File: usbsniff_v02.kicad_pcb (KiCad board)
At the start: 2 copper layers, 40 x 90 mm, 23 parts, among them P1 CONN_01X02, P2 CONN_01X08, P3 CONN_01X08, U1 AMS1117, U2 MAX3421E, U3 MAX3421E, X1 USB_type_A, X2 micro_USB, Y1 Crystal_Small, Y2 Crystal_Small

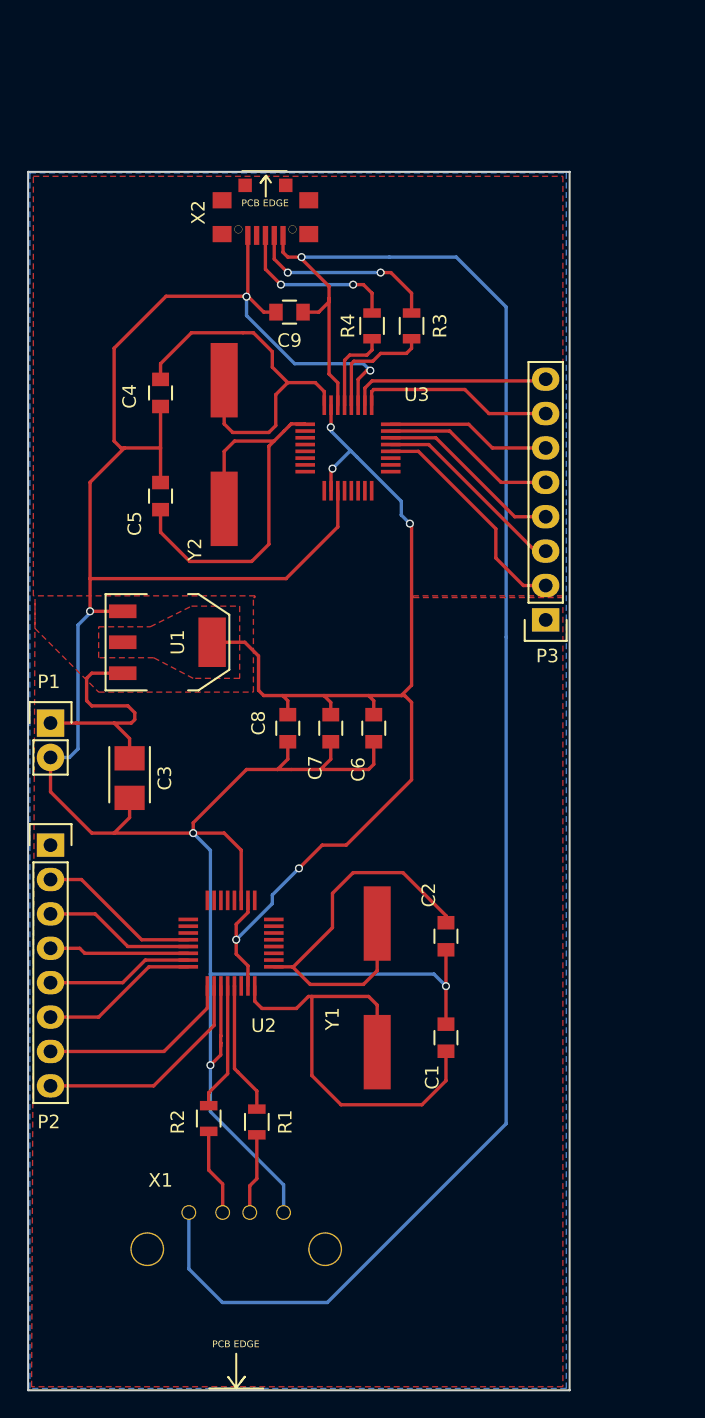
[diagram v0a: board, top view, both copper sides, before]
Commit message: add LED, redesign pcb
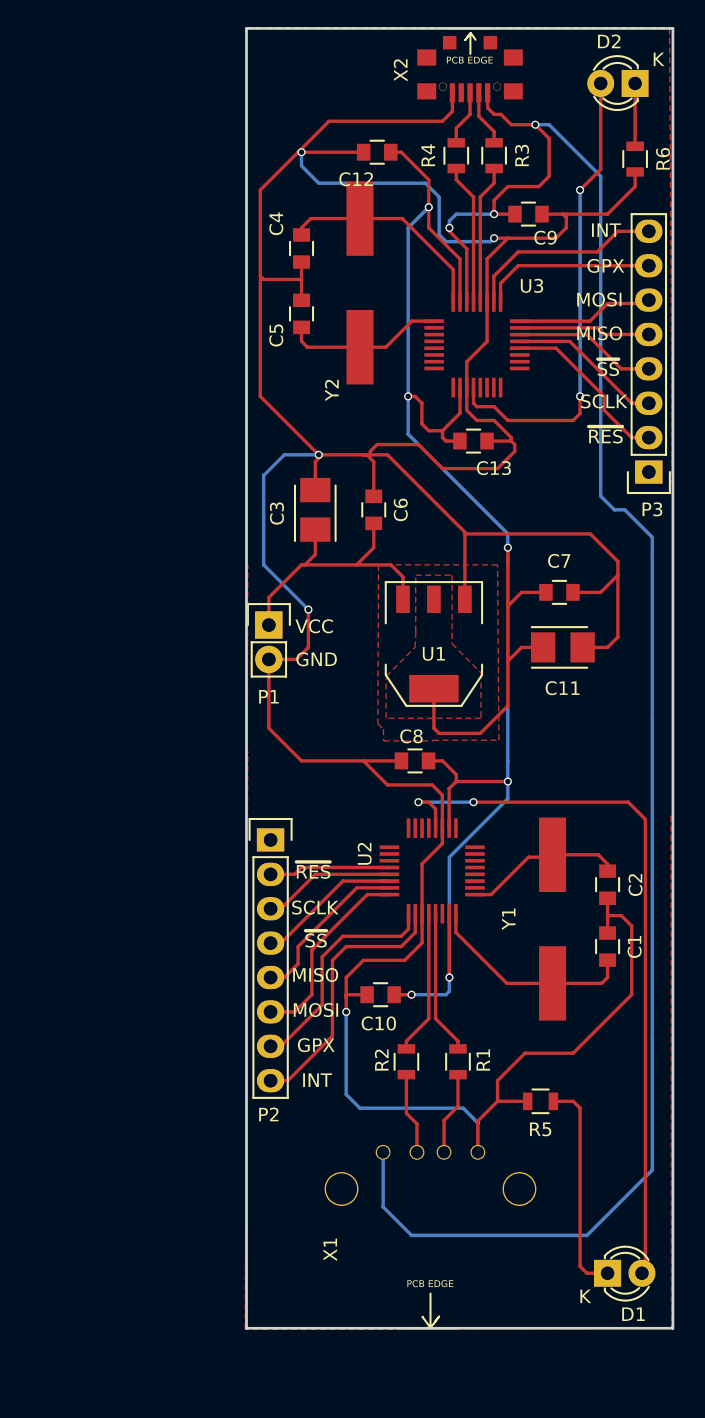
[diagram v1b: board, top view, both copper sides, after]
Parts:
- added C10: 1uF, Capacitors_SMD:C_0805, F.Cu at (66.0, 160.8)
- added C11: 10uF, Capacitors_Tantalum_SMD:TantalC_SizeB_EIA-3528_Reflow, F.Cu at (79.5, 135.1)
- added C12: 1uF, Capacitors_SMD:C_0805, F.Cu at (65.8, 98.6)
- added C13: 0.1uF, Capacitors_SMD:C_0805, F.Cu at (72.9, 119.9)
- added D1: LED, LEDs:LED-3MM, F.Cu at (82.8, 181.4)
- added D2: LED, LEDs:LED-3MM, F.Cu at (84.8, 93.5)
- added R5: 470 Ohm, Resistors_SMD:R_0805, F.Cu at (77.9, 168.7)
- added R6: 470 Ohm, Resistors_SMD:R_0805, F.Cu at (84.8, 99.1)
- C1, C2, C4, C5: value C_Small -> 20pF
- C3: value CP_Small -> 10uF
- C6, C7, C8: value C_Small -> 0.1uF
- C9: value C_Small -> 1uF
- R1, R2, R3, R4: value R_Small -> 33 Ohm
- Y1, Y2: value Crystal_Small -> 12MHz
- moved C3 24.1 mm to (61.2, 125.0), turned to 90 degrees
- moved U1 19.7 mm to (70.0, 134.9), turned to 180 degrees
- moved C7 19.6 mm to (79.2, 131.1), turned to 0 degrees
- moved C9 19.1 mm to (77.0, 103.1), turned to 0 degrees
- moved X2 18.4 mm to (72.6, 89.4)
- moved P1 17.7 mm to (57.8, 133.5)
- moved C5 17.0 mm to (60.2, 110.5)
- moved P2 16.3 mm to (57.9, 149.4)
- moved C6 16.1 mm to (65.5, 125.0), turned to 90 degrees
- moved U2 15.8 mm to (69.8, 151.6)
- moved Y2 15.6 mm to (64.5, 108.2)
- moved R1 15.5 mm to (71.8, 165.7)
- moved R2 15.2 mm to (67.9, 165.7)
- moved X1 15.0 mm to (69.7, 175.1)
- moved C4 14.9 mm to (60.2, 105.7)
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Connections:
- net Net-(C9-Pad1) renamed /ed_VBCOMP
- net Net-(P2-Pad2) renamed /RES_ehost
- net Net-(P3-Pad2) renamed /RES_edevice
- net Net-(R1-Pad1) renamed /ehost_DP
- net Net-(R2-Pad1) renamed /ehost_DM
- net Net-(R3-Pad2) renamed /edevice_DM
- net Net-(R4-Pad2) renamed /edevice_DP
- C6 pad 1: /Vcc_3.3V -> Net-(C3-Pad1)
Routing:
- net GND: track 208.9 -> 283.7 mm, vias 6 -> 5
- net Net-(D1-Pad2): track 0.00 -> 53.8 mm, vias 0 -> 2
- net /Vcc_3.3V: track 81.7 -> 134.1 mm, vias 5 -> 6
- net Net-(D2-Pad2): track 0.00 -> 34.8 mm, vias 0 -> 2
- net /XI_host: track 34.1 -> 15.6 mm
- net /XO_device: track 29.9 -> 11.8 mm
- net /XO_host: track 29.7 -> 11.8 mm
- net Net-(D1-Pad1): track 0.00 -> 16.1 mm
- net /XI_device: track 28.7 -> 16.0 mm
- net Net-(R3-Pad1): track 14.4 -> 4.17 mm, vias 2 -> 0
- net Net-(R4-Pad1): track 12.6 -> 4.12 mm, vias 2 -> 0
- net /ed_VBCOMP: track 128.4 -> 135.4 mm, vias 1 -> 3
- net Net-(D2-Pad1): track 0.00 -> 4.64 mm
- net /RES_edevice: track 16.8 -> 12.9 mm
- net /edevice_DP: track 6.50 -> 10.4 mm
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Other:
- board size 40 x 90 mm -> 31.5 x 96 mm
- board text added: "GND"
- board text added: "GPX"
- board text added: "INT"
- board text added: "MISO"
- board text added: "MOSI"
- board text added: "SCLK"
- board text added: "VCC"
- board text added: "~RES"
- board text added: "~SS"

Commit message: redesign wires
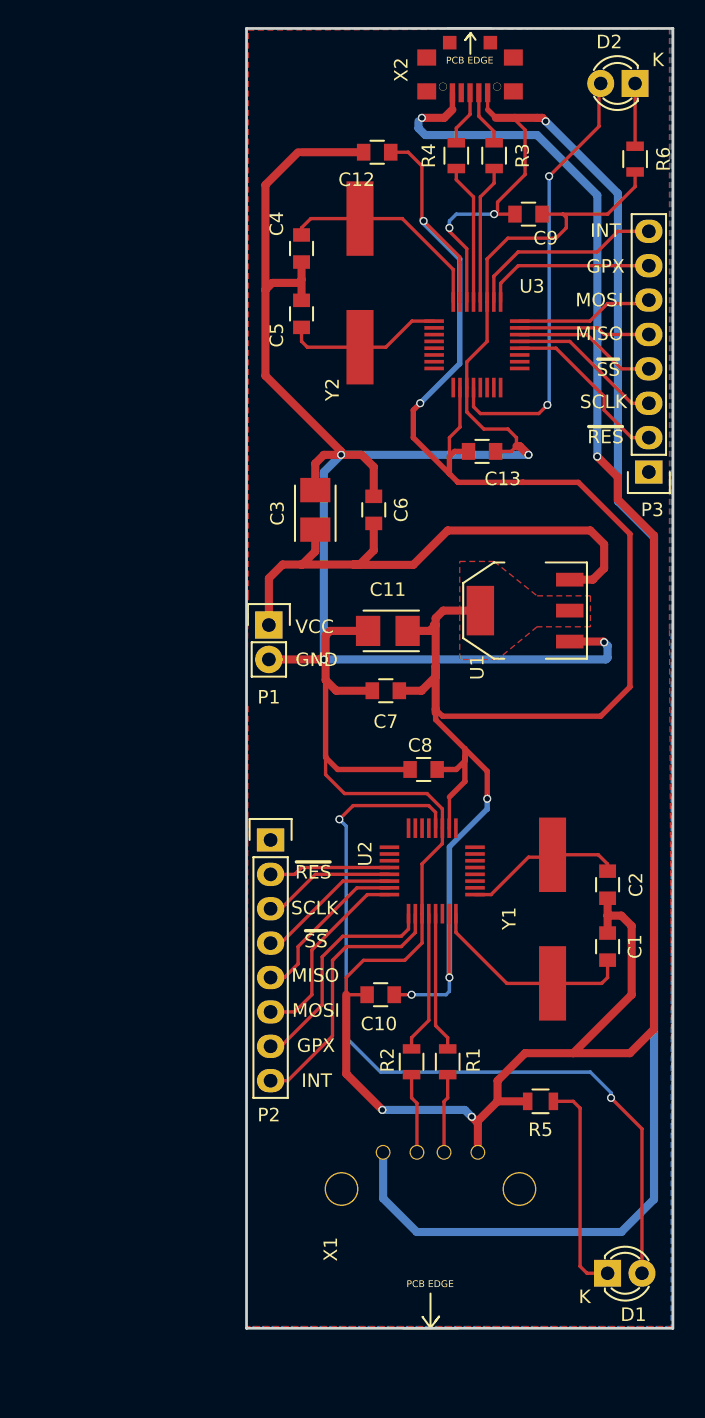
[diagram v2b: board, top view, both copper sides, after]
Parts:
- moved C7 14.7 mm to (66.4, 138.3), turned to 180 degrees
- moved C11 13.0 mm to (66.6, 133.9), turned to 180 degrees
- moved U1 7.17 mm to (76.7, 132.4), turned to 90 degrees
- moved C13 0.99 mm to (73.5, 120.7)
- moved C8 0.90 mm to (69.2, 144.1)
- moved R1 0.76 mm to (71.0, 165.7)
- moved R2 0.38 mm to (68.3, 165.7)
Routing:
- net GND: track 283.7 -> 332.5 mm, vias 5 -> 8
- net Net-(C3-Pad1): track 21.5 -> 41.8 mm
- net /Vcc_3.3V: track 134.1 -> 144.8 mm, vias 6 -> 5
- net Net-(D1-Pad2): track 53.8 -> 61.1 mm
- net Net-(D2-Pad2): track 34.8 -> 32.7 mm
- net /ed_VBCOMP: track 135.4 -> 134.4 mm

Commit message: fix polygon around ams1117
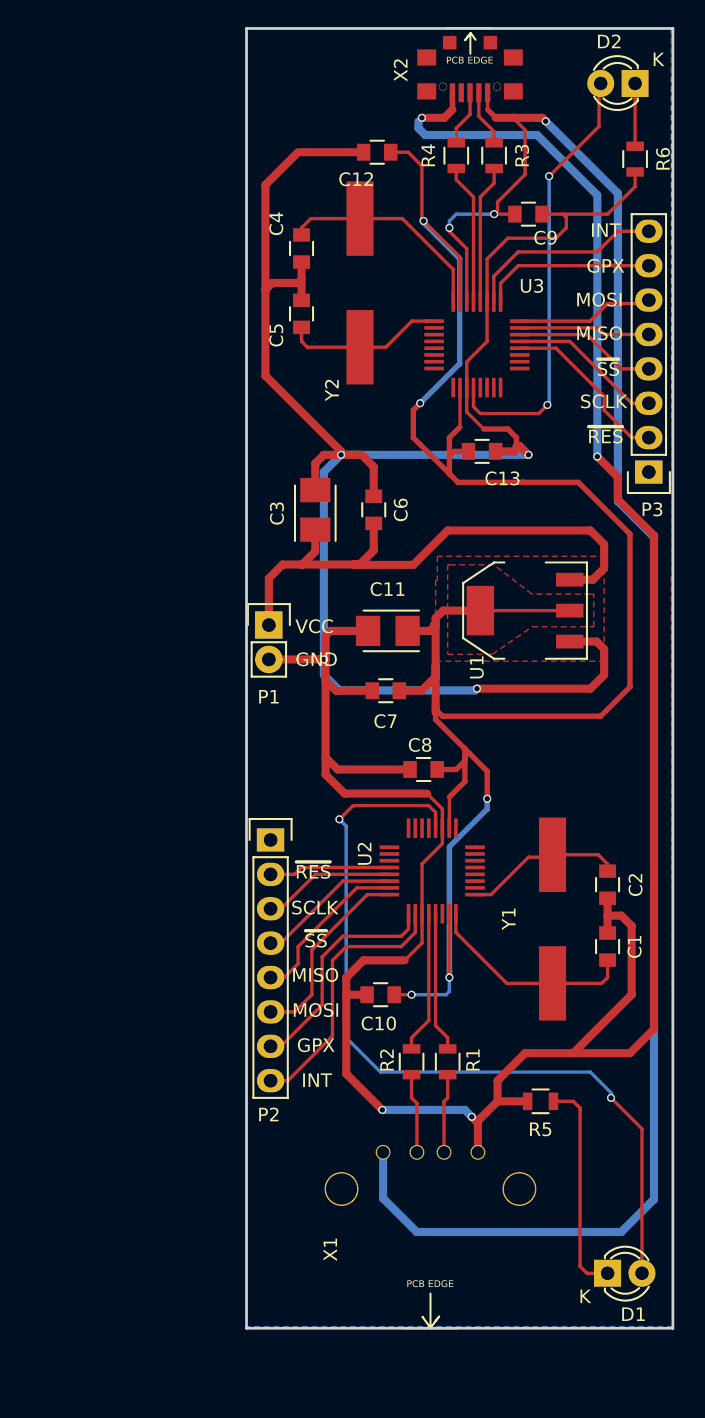
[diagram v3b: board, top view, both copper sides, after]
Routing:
- net /Vcc_3.3V: track 144.8 -> 151.4 mm
- net GND: track 332.5 -> 335.4 mm
